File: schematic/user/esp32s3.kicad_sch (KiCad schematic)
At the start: 15 parts, among them J4 I2C Breakout, J6 ESP32_UART0, J7 MCU Power, J8 ULP Serial, SW1 ESP32S3 Reset, SW2 ESP32S3 Boot Method, U5 ESP32-S3-WROOM-1-N16R8

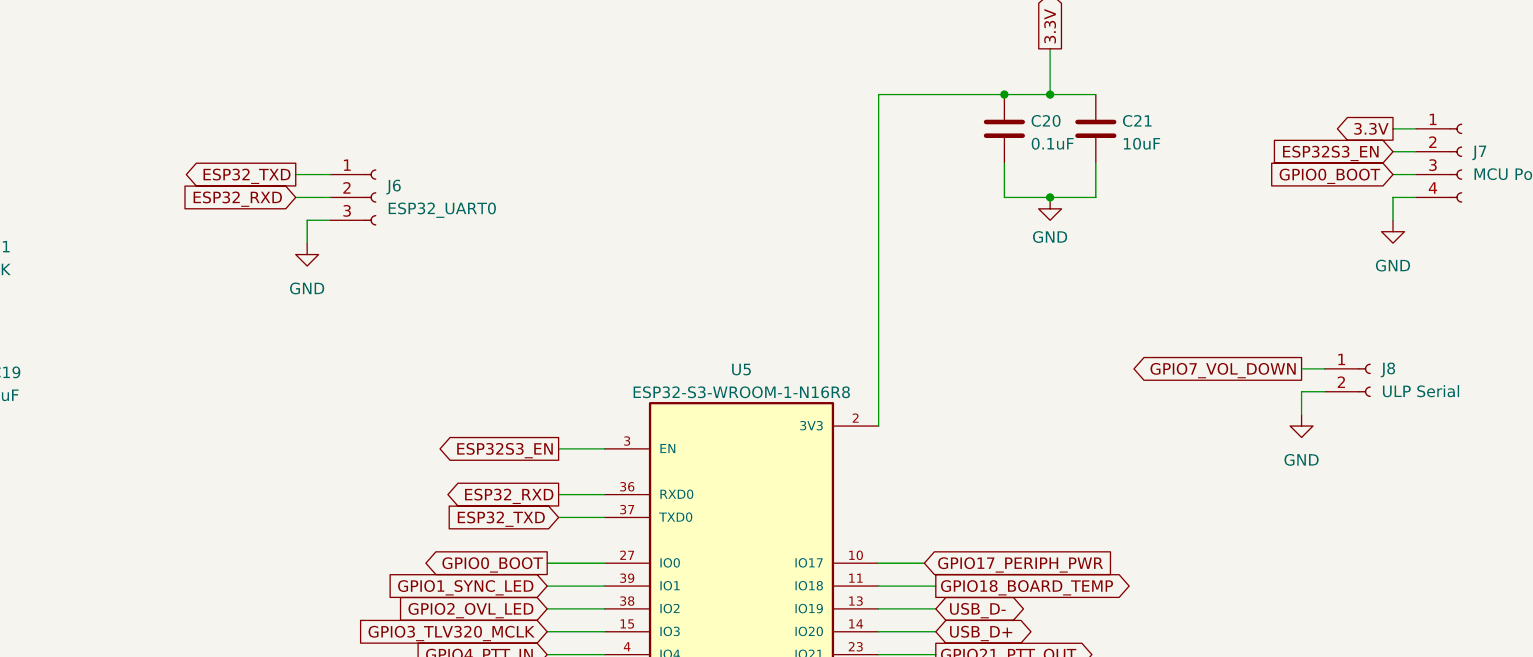
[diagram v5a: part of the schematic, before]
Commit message: v0.6 board: Reroute headers on LHS to allow access to all buttons.
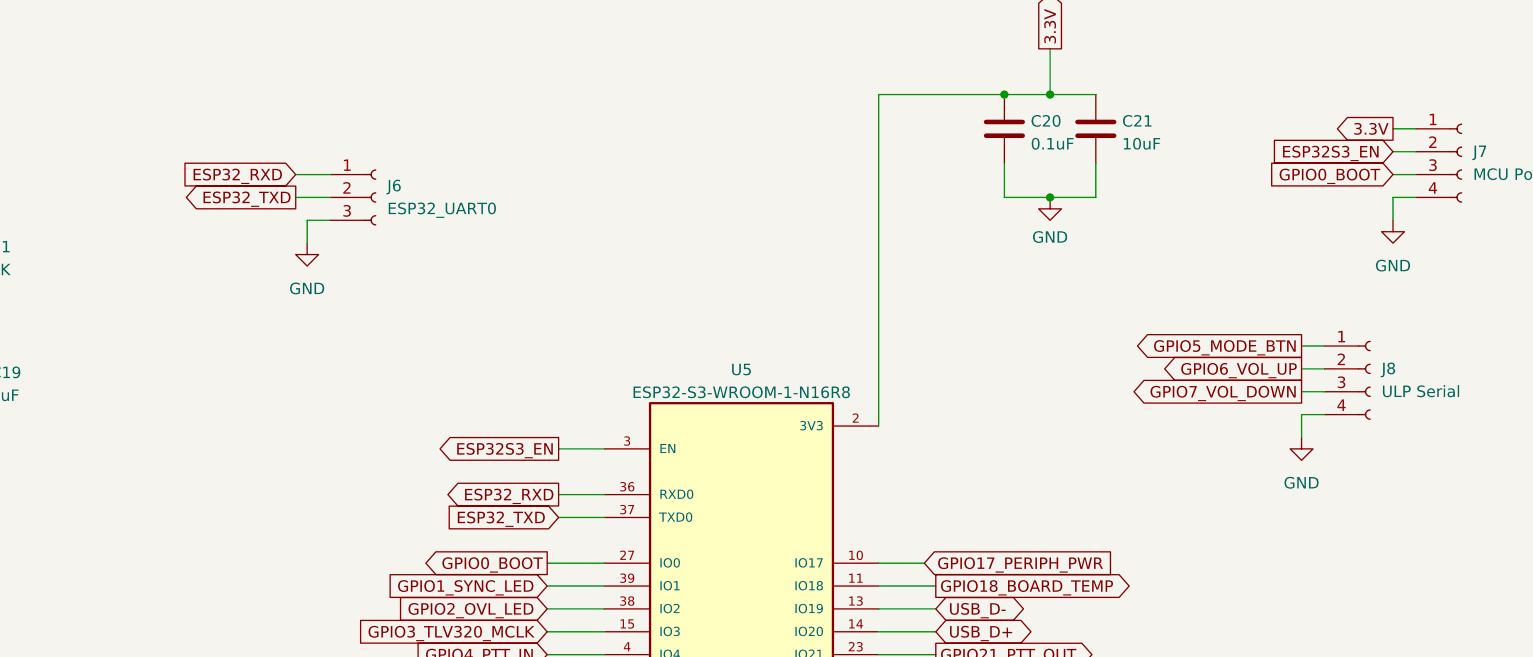
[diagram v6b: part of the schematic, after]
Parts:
- J8: footprint Connector_PinHeader_2.54mm:PinHeader_1x02_P2.54mm_Vertical -> Connector_PinHeader_2.54mm:PinHeader_2x02_P2.54mm_Vertical; symbol Connector:Conn_01x02_Female -> Connector:Conn_01x04_Female
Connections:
- net ESP32_RXD: now also J6.1 (Pin_1); no longer J6.2 (Pin_2)
- net ESP32_TXD: now also J6.2 (Pin_2); no longer J6.1 (Pin_1)
- net GND: now also J8.4 (Pin_4); no longer J8.2 (Pin_2)
- net GPIO5_MODE_BTN: now also J8.1 (Pin_1)
- net GPIO6_VOL_UP: now also J8.2 (Pin_2)
- net GPIO7_VOL_DOWN: now also J8.3 (Pin_3); no longer J8.1 (Pin_1)
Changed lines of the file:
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@@
-    (stroke (width 0) (type default) (color 0 0 0 0))
-  )
-  (wire (pts (xy 237.49 66.04) (xy 234.95 66.04))
     (stroke (width 0) (type default) (color 0 0 0 0))
   )
@@
     (stroke (width 0) (type default) (color 0 0 0 0))
   )
+  (wire (pts (xy 234.95 71.12) (xy 234.95 68.58))
+    (stroke (width 0) (type default) (color 0 0 0 0))
+  )
   (wire (pts (xy 123.19 41.91) (xy 127 41.91))
     (stroke (width 0) (type default) (color 0 0 0 0))
   )
+  (wire (pts (xy 234.95 60.96) (xy 237.49 60.96))
+    (stroke (width 0) (type default) (color 0 0 0 0))
+  )
   (wire (pts (xy 152.4 72.39) (xy 157.48 72.39))
     (stroke (width 0) (type default) (color 0 0 0 0))
@@
     (stroke (width 0) (type default) (color 0 0 0 0))
   )
+  (wire (pts (xy 234.95 66.04) (xy 237.49 66.04))
+    (stroke (width 0) (type default) (color 0 0 0 0))
+  )
+  (wire (pts (xy 234.95 68.58) (xy 237.49 68.58))
+    (stroke (width 0) (type default) (color 0 0 0 0))
+  )
   (wire (pts (xy 80.01 58.42) (xy 86.36 58.42))
     (stroke (width 0) (type default) (color 0 0 0 0))
@@
     (stroke (width 0) (type default) (color 0 0 0 0))
   )
-  (wire (pts (xy 234.95 66.04) (xy 234.95 68.58))
-    (stroke (width 0) (type default) (color 0 0 0 0))
-  )
   (wire (pts (xy 151.13 120.65) (xy 157.48 120.65))
     (stroke (width 0) (type default) (color 0 0 0 0))
@@
     )
   )
-  (global_label "ESP32_TXD" (shape output) (at 123.19 41.91 180) (fields_autoplaced)
-    (effects (font (size 1.27 1.27)) (justify right))
-    (property "Intersheet References" "${INTERSHEET_REFS}" (id 0) (at 110.3145 41.8306 0)
+  (global_label "ESP32_TXD" (shape output) (at 123.19 44.45 180) (fields_autoplaced)
+    (effects (font (size 1.27 1.27)) (justify right))
+    (property "Intersheet References" "${INTERSHEET_REFS}" (id 0) (at 110.3145 44.3706 0)
       (effects (font (size 1.27 1.27)) (justify right) hide)
     )
@@
     )
   )
-  (global_label "GPIO7_VOL_DOWN" (shape output) (at 234.95 63.5 180) (fields_autoplaced)
-    (effects (font (size 1.27 1.27)) (justify right))
-    (property "Intersheet References" "${INTERSHEET_REFS}" (id 0) (at 216.0874 63.4206 0)
-      (effects (font (size 1.27 1.27)) (justify right) hide)
-    )
-  )
-  (global_label "ESP32_RXD" (shape input) (at 123.19 44.45 180) (fields_autoplaced)
-    (effects (font (size 1.27 1.27)) (justify right))
-    (property "Intersheet References" "${INTERSHEET_REFS}" (id 0) (at 110.0121 44.3706 0)
+  (global_label "GPIO7_VOL_DOWN" (shape output) (at 234.95 66.04 180) (fields_autoplaced)
+    (effects (font (size 1.27 1.27)) (justify right))
+    (property "Intersheet References" "${INTERSHEET_REFS}" (id 0) (at 216.0874 65.9606 0)
+      (effects (font (size 1.27 1.27)) (justify right) hide)
+    )
+  )
+  (global_label "ESP32_RXD" (shape input) (at 123.19 41.91 180) (fields_autoplaced)
+    (effects (font (size 1.27 1.27)) (justify right))
+    (property "Intersheet References" "${INTERSHEET_REFS}" (id 0) (at 110.0121 41.8306 0)
       (effects (font (size 1.27 1.27)) (justify right) hide)
     )
@@
     )
   )
+  (global_label "GPIO5_MODE_BTN" (shape output) (at 234.95 60.96 180) (fields_autoplaced)
+    (effects (font (size 1.27 1.27)) (justify right))
+    (property "Intersheet References" "${INTERSHEET_REFS}" (id 0) (at 216.1479 60.8806 0)
+      (effects (font (size 1.27 1.27)) (justify right) hide)
+    )
+  )
   (global_label "3.3V_PERIPH" (shape output) (at 74.93 134.62 90) (fields_autoplaced)
     (effects (font (size 1.27 1.27)) (justify left))
@@
     (property "Intersheet References" "${INTERSHEET_REFS}" (id 0) (at 204.3431 90.0906 0)
       (effects (font (size 1.27 1.27)) (justify left) hide)
+    )
+  )
+  (global_label "GPIO6_VOL_UP" (shape output) (at 234.95 63.5 180) (fields_autoplaced)
+    (effects (font (size 1.27 1.27)) (justify right))
+    (property "Intersheet References" "${INTERSHEET_REFS}" (id 0) (at 218.8693 63.4206 0)
+      (effects (font (size 1.27 1.27)) (justify right) hide)
     )
   )
@@
     (pin "2")
   )
-  (symbol (lib_id "Connector:Conn_01x02_Female") (at 242.57 63.5 0) (unit 1)
+  (symbol (lib_id "Connector:Conn_01x04_Female") (at 242.57 63.5 0) (unit 1)
     (in_bom yes) (on_board yes) (fields_autoplaced)
     (property "Reference" "J8" (id 0) (at 243.84 63.4999 0)
@@
       (effects (font (size 1.27 1.27)) (justify left))
     )
-    (property "Footprint" "Connector_PinHeader_2.54mm:PinHeader_1x02_P2.54mm_Vertical" (id 2) (at 242.57 63.5 0)
+    (property "Footprint" "Connector_PinHeader_2.54mm:PinHeader_2x02_P2.54mm_Vertical" (id 2) (at 242.57 63.5 0)
       (effects (font (size 1.27 1.27)) hide)
     )
@@
     (pin "1")
     (pin "2")
+    (pin "3")
+    (pin "4")
   )
   (symbol (lib_id "power:GND") (at 124.46 49.53 0) (unit 1)
@@
     (pin "2")
   )
-  (symbol (lib_id "power:GND") (at 234.95 68.58 0) (unit 1)
-    (in_bom yes) (on_board yes) (fields_autoplaced)
-    (property "Reference" "#PWR045" (id 0) (at 234.95 74.93 0)
-      (effects (font (size 1.27 1.27)) hide)
-    )
-    (property "Value" "GND" (id 1) (at 234.95 73.66 0))
-    (property "Footprint" "" (id 2) (at 234.95 68.58 0)
-      (effects (font (size 1.27 1.27)) hide)
-    )
-    (property "Datasheet" "" (id 3) (at 234.95 68.58 0)
-      (effects (font (size 1.27 1.27)) hide)
-    )
+  (symbol (lib_id "power:GND") (at 234.95 71.12 0) (unit 1)
+    (in_bom yes) (on_board yes) (fields_autoplaced)
+    (property "Reference" "#PWR045" (id 0) (at 234.95 77.47 0)
+      (effects (font (size 1.27 1.27)) hide)
+    )
+    (property "Value" "GND" (id 1) (at 234.95 76.2 0))
+    (property "Footprint" "" (id 2) (at 234.95 71.12 0)
+      (effects (font (size 1.27 1.27)) hide)
+    )
+    (property "Datasheet" "" (id 3) (at 234.95 71.12 0)
+      (effects (font (size 1.27 1.27)) hide)
+    )

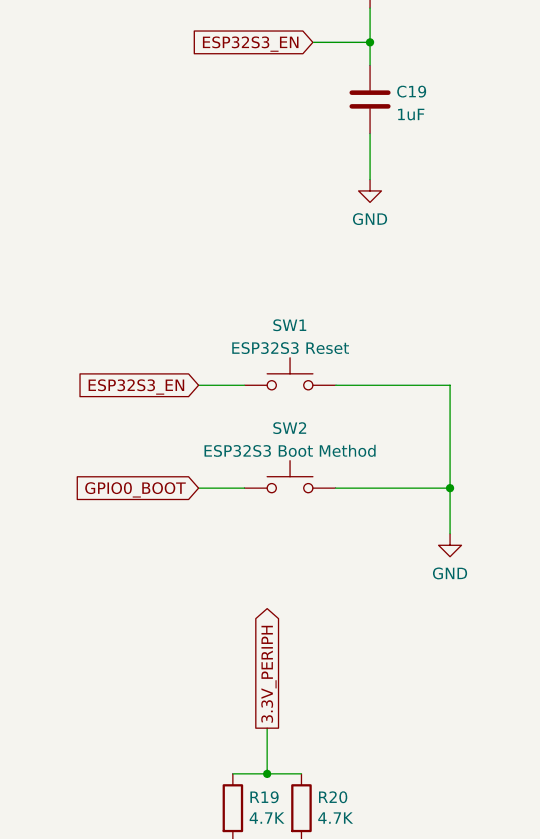
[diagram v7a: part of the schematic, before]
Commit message: v0.7 board: add TVS protection for GPIO0/reset.
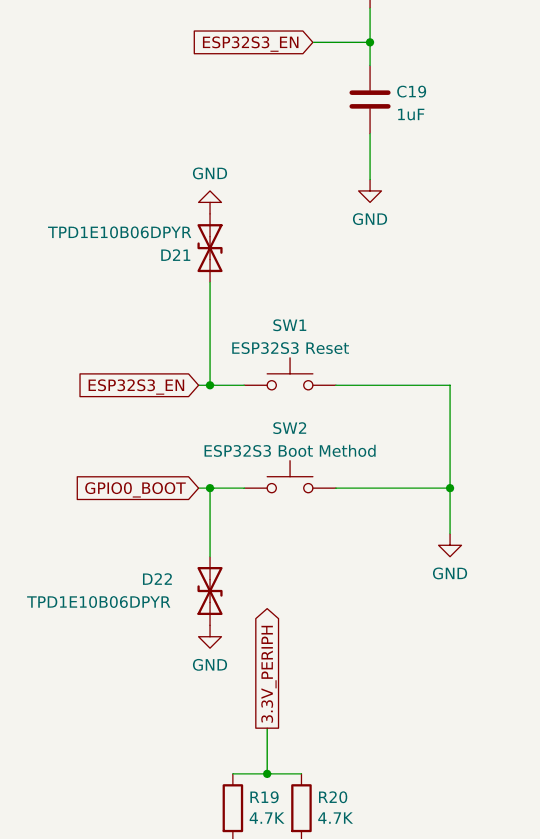
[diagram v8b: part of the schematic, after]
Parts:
- added D21, D22: TPD1E10B06DPYR, ezDV_production:DIO_TPD1E05U06DPYR, symbol Device:D_TVS
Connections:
- net ESP32S3_EN: now also D21.2 (A2)
- net GND: now also D21.1 (A1), D22.1 (A1)
- net GPIO0_BOOT: now also D22.2 (A2)
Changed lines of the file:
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@@
   (junction (at 71.12 149.86) (diameter 0) (color 0 0 0 0)
+  )
+  (junction (at 68.58 107.95) (diameter 0) (color 0 0 0 0)
+  )
+  (junction (at 68.58 96.52) (diameter 0) (color 0 0 0 0)
   )
   (junction (at 86.36 58.42) (diameter 0) (color 0 0 0 0)
@@
     (stroke (width 0) (type default) (color 0 0 0 0))
   )
-  (wire (pts (xy 67.31 107.95) (xy 72.39 107.95))
+  (wire (pts (xy 67.31 107.95) (xy 68.58 107.95))
+    (stroke (width 0) (type default) (color 0 0 0 0))
+  )
+  (wire (pts (xy 68.58 96.52) (xy 72.39 96.52))
     (stroke (width 0) (type default) (color 0 0 0 0))
   )
@@
     (stroke (width 0) (type default) (color 0 0 0 0))
   )
+  (wire (pts (xy 68.58 85.09) (xy 68.58 96.52))
+    (stroke (width 0) (type default) (color 0 0 0 0))
+  )
   (wire (pts (xy 201.93 40.64) (xy 201.93 44.45))
     (stroke (width 0) (type default) (color 0 0 0 0))
@@
     (stroke (width 0) (type default) (color 0 0 0 0))
   )
+  (wire (pts (xy 68.58 107.95) (xy 72.39 107.95))
+    (stroke (width 0) (type default) (color 0 0 0 0))
+  )
   (wire (pts (xy 86.36 41.91) (xy 86.36 46.99))
     (stroke (width 0) (type default) (color 0 0 0 0))
@@
     (stroke (width 0) (type default) (color 0 0 0 0))
   )
-  (wire (pts (xy 67.31 96.52) (xy 72.39 96.52))
+  (wire (pts (xy 67.31 96.52) (xy 68.58 96.52))
     (stroke (width 0) (type default) (color 0 0 0 0))
   )
@@
   )
   (wire (pts (xy 86.36 58.42) (xy 86.36 60.96))
+    (stroke (width 0) (type default) (color 0 0 0 0))
+  )
+  (wire (pts (xy 68.58 107.95) (xy 68.58 115.57))
     (stroke (width 0) (type default) (color 0 0 0 0))
   )
@@
     (pin "1")
   )
+  (symbol (lib_id "power:GND") (at 68.58 123.19 0) (unit 1)
+    (in_bom yes) (on_board yes) (fields_autoplaced)
+    (property "Reference" "#PWR063" (id 0) (at 68.58 129.54 0)
+      (effects (font (size 1.27 1.27)) hide)
+    )
+    (property "Value" "GND" (id 1) (at 68.58 127.6334 0))
+    (property "Footprint" "" (id 2) (at 68.58 123.19 0)
+      (effects (font (size 1.27 1.27)) hide)
+    )
+    (property "Datasheet" "" (id 3) (at 68.58 123.19 0)
+      (effects (font (size 1.27 1.27)) hide)
+    )
+    (pin "1")
+  )
   (symbol (lib_id "Connector:Conn_01x04_Female") (at 76.2 166.37 270) (unit 1)
     (in_bom yes) (on_board yes) (fields_autoplaced)
@@
     (pin "2")
   )
+  (symbol (lib_id "Device:D_TVS") (at 68.58 119.38 90) (unit 1)
+    (in_bom yes) (on_board yes)
+    (property "Reference" "D22" (id 0) (at 60.96 118.11 90)
+      (effects (font (size 1.27 1.27)) (justify right))
+    )
+    (property "Value" "TPD1E10B06DPYR" (id 1) (at 48.26 120.65 90)
+      (effects (font (size 1.27 1.27)) (justify right))
+    )
+    (property "Footprint" "ezDV_production:DIO_TPD1E05U06DPYR" (id 2) (at 68.58 119.38 0)
+      (effects (font (size 1.27 1.27)) hide)
+    )
+    (property "Datasheet" "https://www.ti.com/lit/ds/symlink/tpd1e10b06.pdf?ts=1673062853444" (id 3) (at 68.58 119.38 0)
+      (effects (font (size 1.27 1.27)) hide)
+    )
+    (property "LCSC" "C48260" (id 4) (at 68.58 119.38 90)
+      (effects (font (size 1.27 1.27)) hide)
+    )
+    (pin "1")
+    (pin "2")
+  )
   (symbol (lib_id "Connector:Conn_01x04_Female") (at 242.57 63.5 0) (unit 1)
     (in_bom yes) (on_board yes) (fields_autoplaced)
@@
     (pin "2")
   )
+  (symbol (lib_id "power:GND") (at 68.58 77.47 180) (unit 1)
+    (in_bom yes) (on_board yes) (fields_autoplaced)
+    (property "Reference" "#PWR062" (id 0) (at 68.58 71.12 0)
+      (effects (font (size 1.27 1.27)) hide)
+    )
+    (property "Value" "GND" (id 1) (at 68.58 73.0266 0))
+    (property "Footprint" "" (id 2) (at 68.58 77.47 0)
+      (effects (font (size 1.27 1.27)) hide)
+    )
+    (property "Datasheet" "" (id 3) (at 68.58 77.47 0)
+      (effects (font (size 1.27 1.27)) hide)
+    )
+    (pin "1")
+  )
   (symbol (lib_id "Device:C") (at 86.36 64.77 0) (unit 1)
     (in_bom yes) (on_board yes) (fields_autoplaced)
@@
       (effects (font (size 1.27 1.27)) hide)
     )
+    (pin "1")
+    (pin "2")
+  )
+  (symbol (lib_id "Device:D_TVS") (at 68.58 81.28 270) (unit 1)
+    (in_bom yes) (on_board yes) (fields_autoplaced)
+    (property "Reference" "D21" (id 0) (at 66.548 82.1147 90)
+      (effects (font (size 1.27 1.27)) (justify right))
+    )
+    (property "Value" "TPD1E10B06DPYR" (id 1) (at 66.548 79.5778 90)
+      (effects (font (size 1.27 1.27)) (justify right))
+    )
+    (property "Footprint" "ezDV_production:DIO_TPD1E05U06DPYR" (id 2) (at 68.58 81.28 0)
+      (effects (font (size 1.27 1.27)) hide)
+    )
+    (property "Datasheet" "https://www.ti.com/lit/ds/symlink/tpd1e10b06.pdf?ts=1673062853444" (id 3) (at 68.58 81.28 0)
+      (effects (font (size 1.27 1.27)) hide)
+    )
+    (property "LCSC" "C48260" (id 4) (at 68.58 81.28 90)
+      (effects (font (size 1.27 1.27)) hide)
+    )
